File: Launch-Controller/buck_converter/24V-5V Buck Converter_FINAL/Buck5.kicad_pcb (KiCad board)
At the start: 4 copper layers, 30.5 x 45.8 mm, 14 parts, among them J1 Conn_01x10_Socket, U1 LM2596S-5

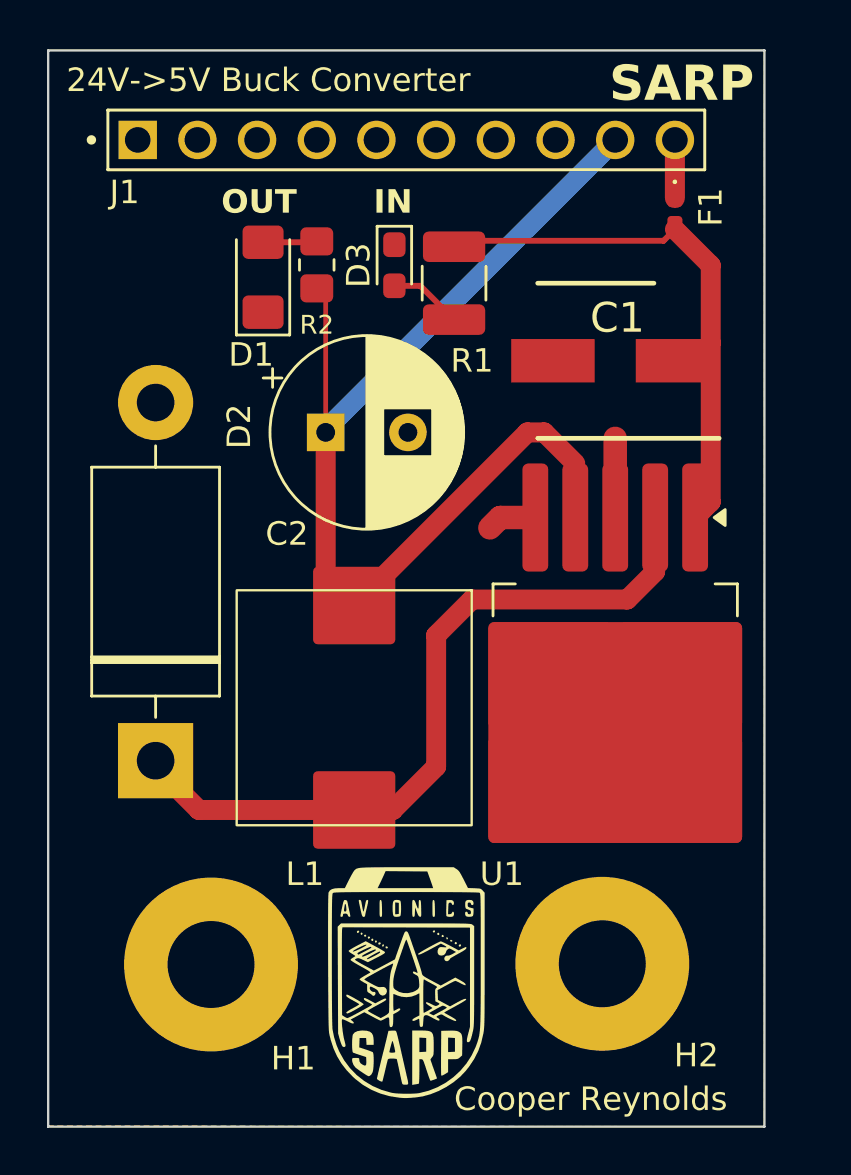
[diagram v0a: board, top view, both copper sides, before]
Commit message: via threading buck converter
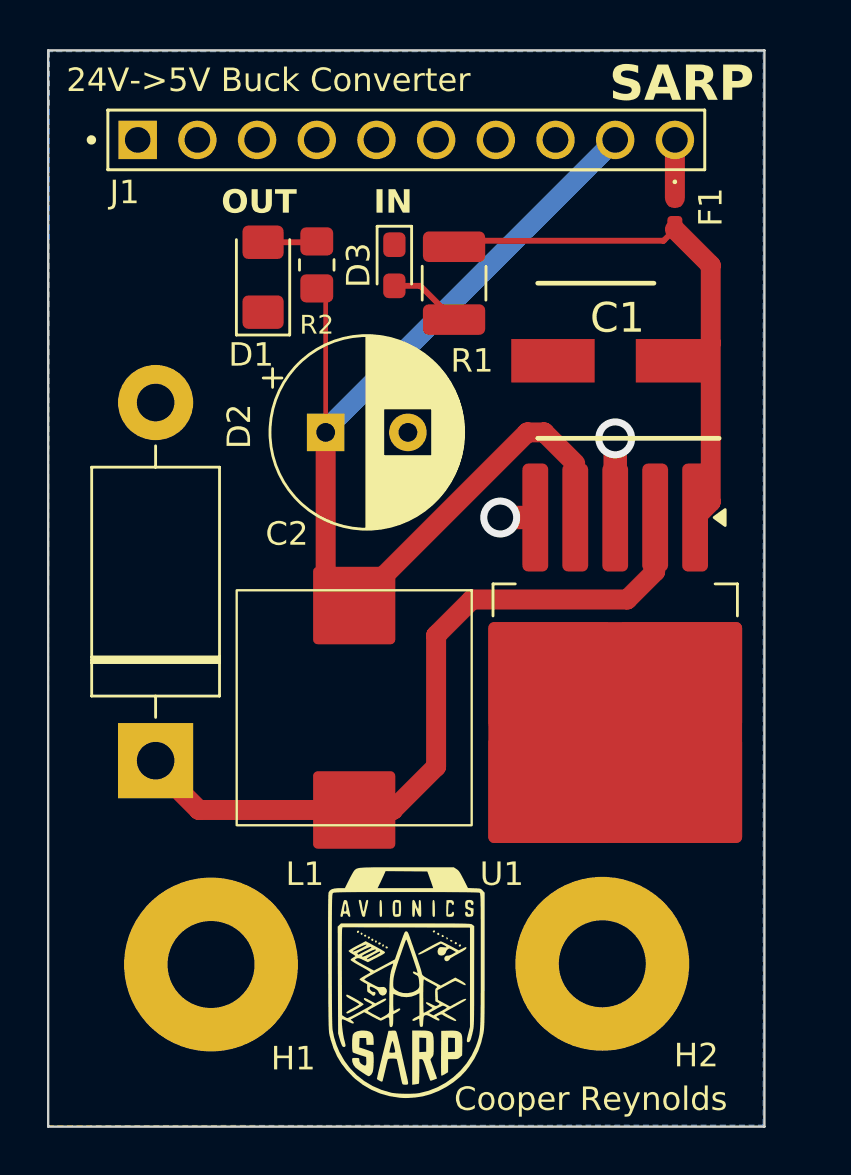
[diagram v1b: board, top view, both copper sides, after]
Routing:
- net GND: track 5.49 -> 4.86 mm, vias 0 -> 2
- added copper zone on B.Cu, net GND
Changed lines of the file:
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@@
 			(drillshape 0)
 			(scaleselection 1)
-			(outputdirectory "")
+			(outputdirectory "Buck_Gerber/")
 		)
 	)
@@
 		(net 6)
 	)
-	(segment
-		(start 115.757 89.729)
-		(end 115.316 90.17)
-		(width 1)
-		(layer "F.Cu")
+	(via
+		(at 120.65 86.36)
+		(size 1.7)
+		(drill 1.1)
+		(layers "F.Cu" "B.Cu")
+		(net 6)
+	)
+	(via
+		(at 115.757 89.729)
+		(size 1.7)
+		(drill 1.1)
+		(layers "F.Cu" "B.Cu")
 		(net 6)
 	)
@@
 			)
 		)
+	)
+	(zone
+		(net 6)
+		(net_name "GND")
+		(layer "B.Cu")
+		(hatch edge 0.5)
+		(priority 1)
+		(connect_pads
+			(clearance 0.5)
+		)
+		(min_thickness 0.25)
+		(filled_areas_thickness no)
+		(fill yes
+			(thermal_gap 0.5)
+			(thermal_bridge_width 0.5)
+		)
+		(polygon
+			(pts
+				(xy 96.50312 115.610089) (xy 126.949238 115.588854) (xy 126.94884 69.899985) (xy 96.569549 69.900244)
+				(xy 96.504004 115.609729) (xy 96.52 115.57)
+			)
+		)
